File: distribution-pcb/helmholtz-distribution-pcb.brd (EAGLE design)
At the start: 100 x 67 mm, 32 parts, among them J1 RASPBERRYPI-40-PIN-GPIO_PTH

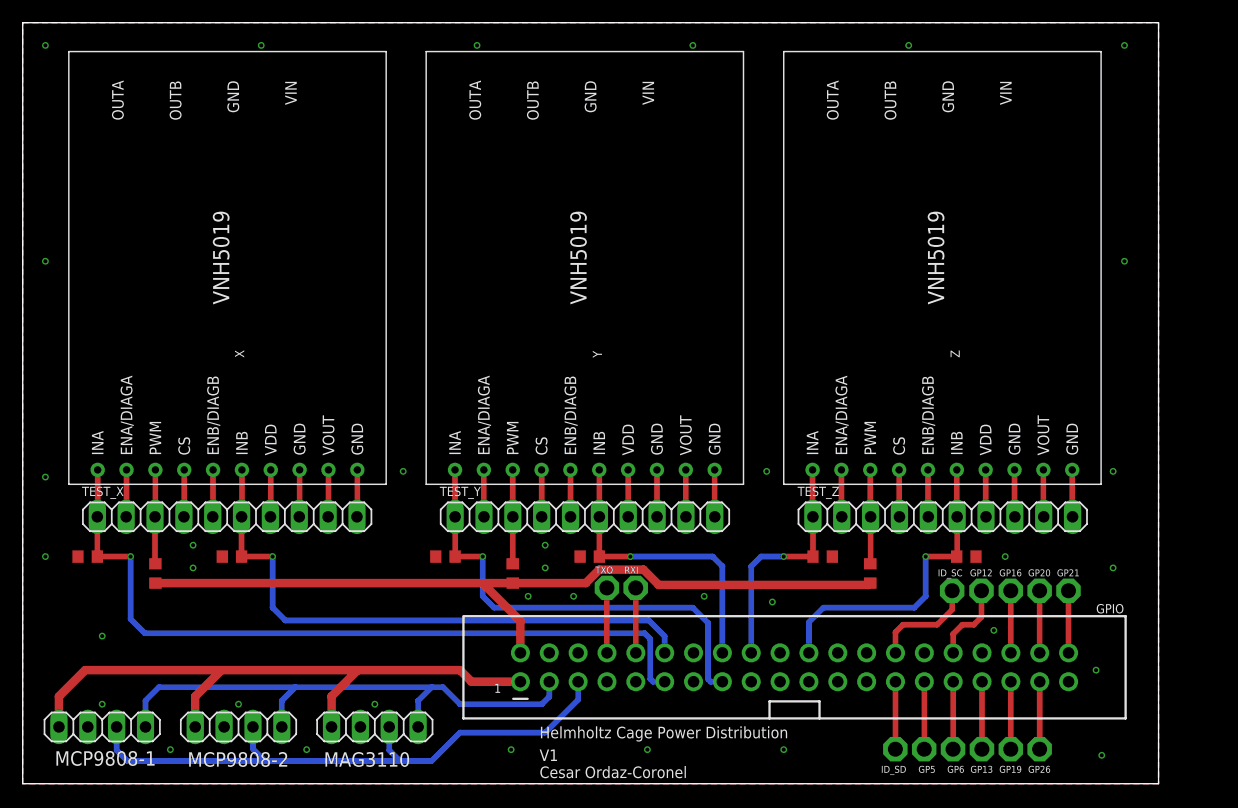
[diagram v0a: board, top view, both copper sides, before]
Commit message: Added mounting holes to VNH boards, put mounting holes on board, and changed font to vector.
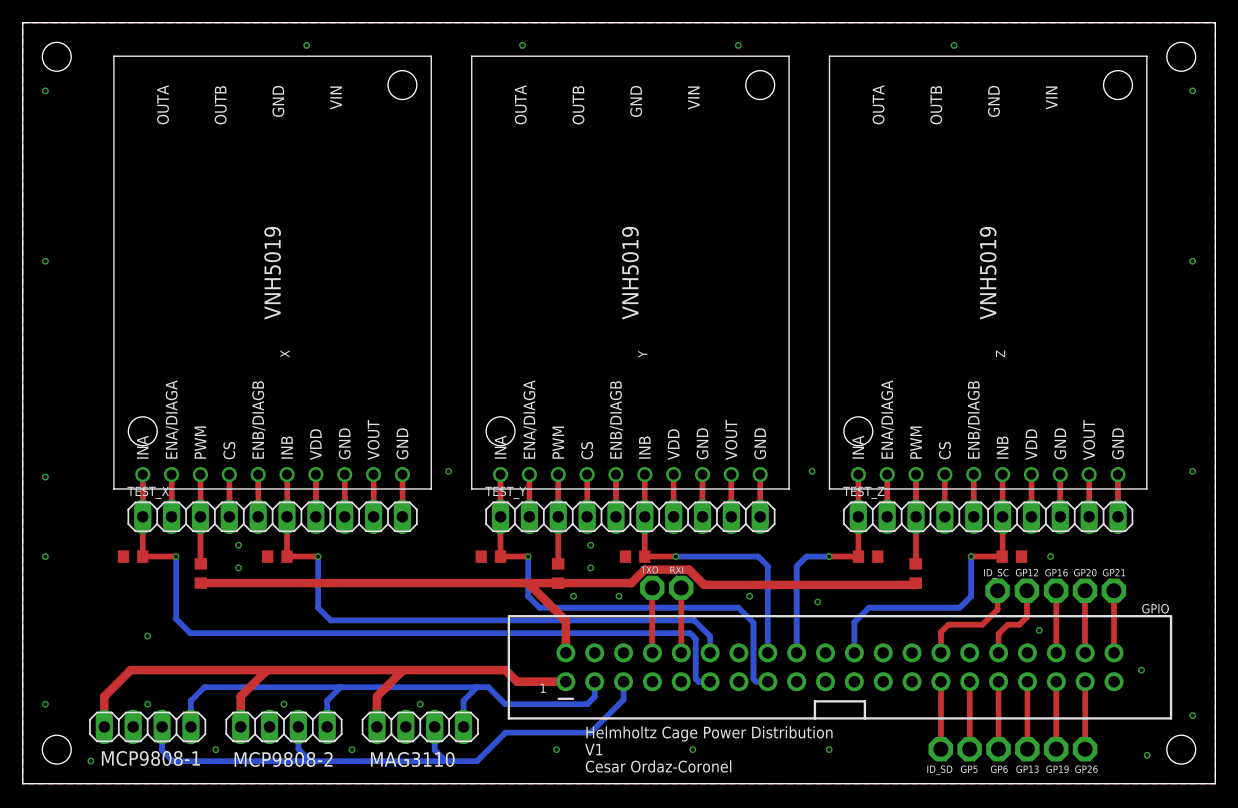
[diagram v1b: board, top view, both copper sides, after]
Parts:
- moved Z 26.5 mm to (85.0, 45.0)
- moved Y 26.5 mm to (53.5, 45.0)
- moved X 26.5 mm to (22.0, 45.0)
- moved R17 4.00 mm to (9.72, 20.0)
- moved GP12 4.00 mm to (88.4, 17.0)
- moved GP13 4.00 mm to (88.5, 3.04)
- moved GP16 4.00 mm to (91.0, 17.0)
- moved GP19 4.00 mm to (91.0, 3.04)
- moved GP20 4.00 mm to (93.5, 17.0)
- moved GP21 4.00 mm to (96.1, 17.0)
- moved GP26 4.00 mm to (93.5, 3.04)
- moved GP5 4.00 mm to (83.4, 3.04)
- moved GP6 4.00 mm to (85.9, 3.04)
- moved ID_SC 4.00 mm to (85.8, 17.0)
- moved ID_SD 4.00 mm to (80.8, 3.04)
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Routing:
- net GND: track 24.8 -> 22.4 mm, vias 35 -> 37
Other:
- board size 100 x 67 mm -> 105 x 67 mm
